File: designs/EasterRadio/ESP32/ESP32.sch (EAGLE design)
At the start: 25 parts, among them IC6 ESP32-WROVER-B, J3 S2B-NSHSS-TB, J5 S2B-NSHSS-TB

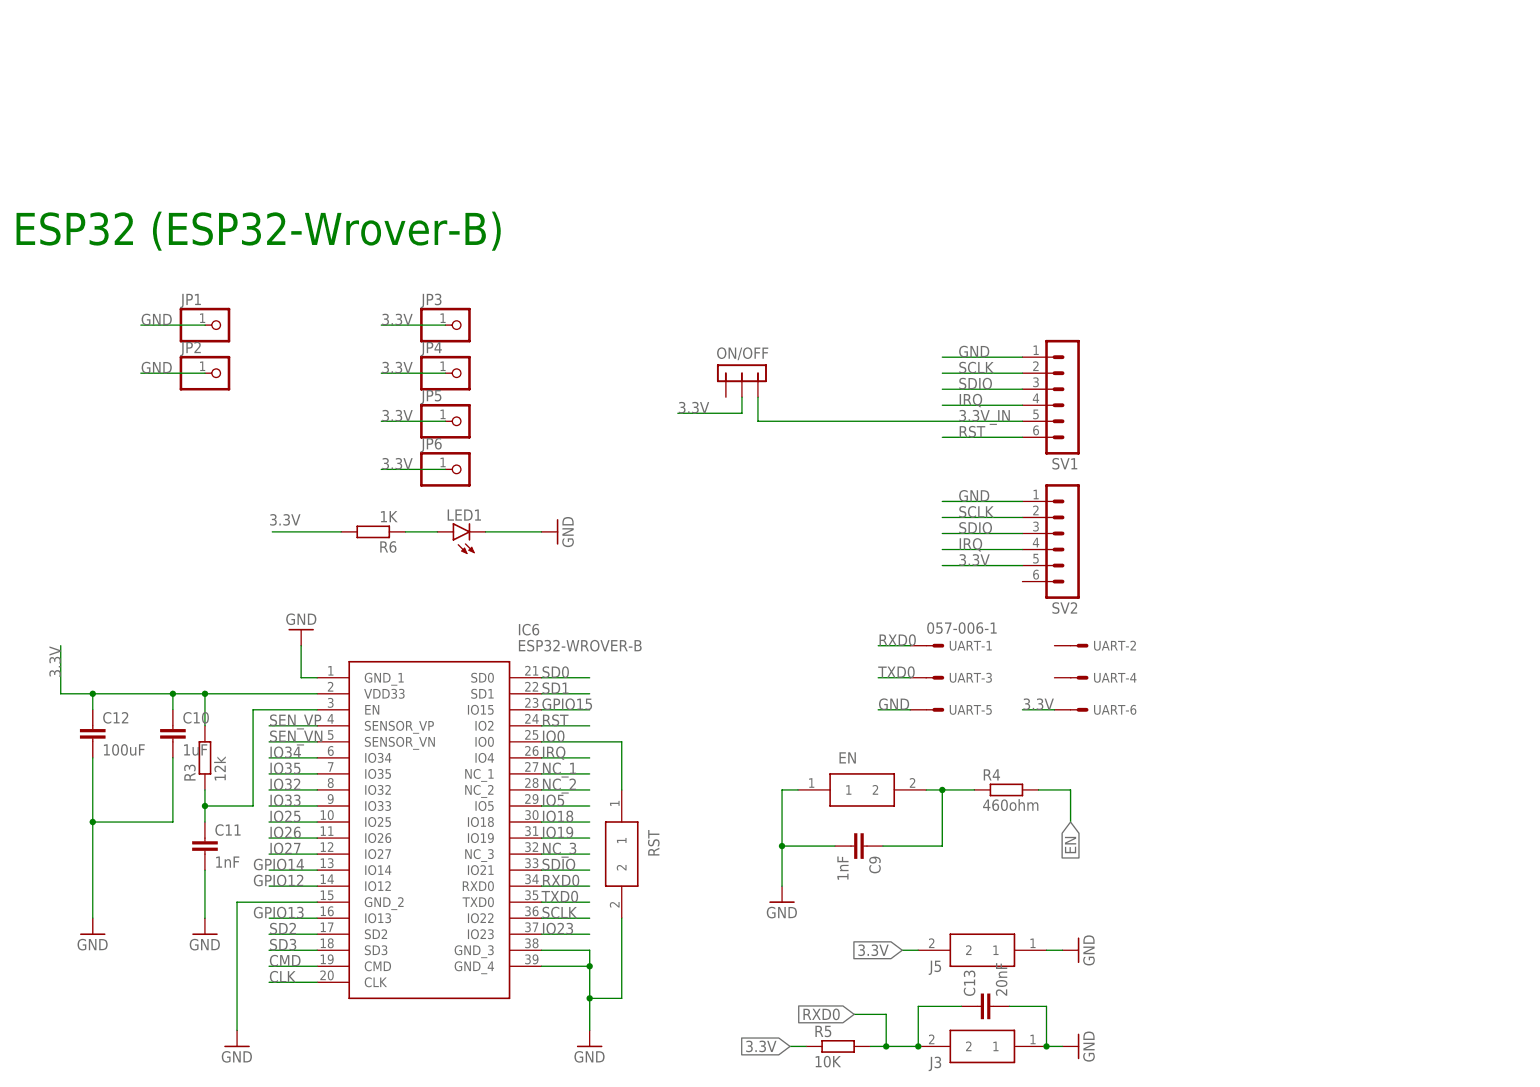
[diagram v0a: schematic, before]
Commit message: added ESP32 wrover E schematic
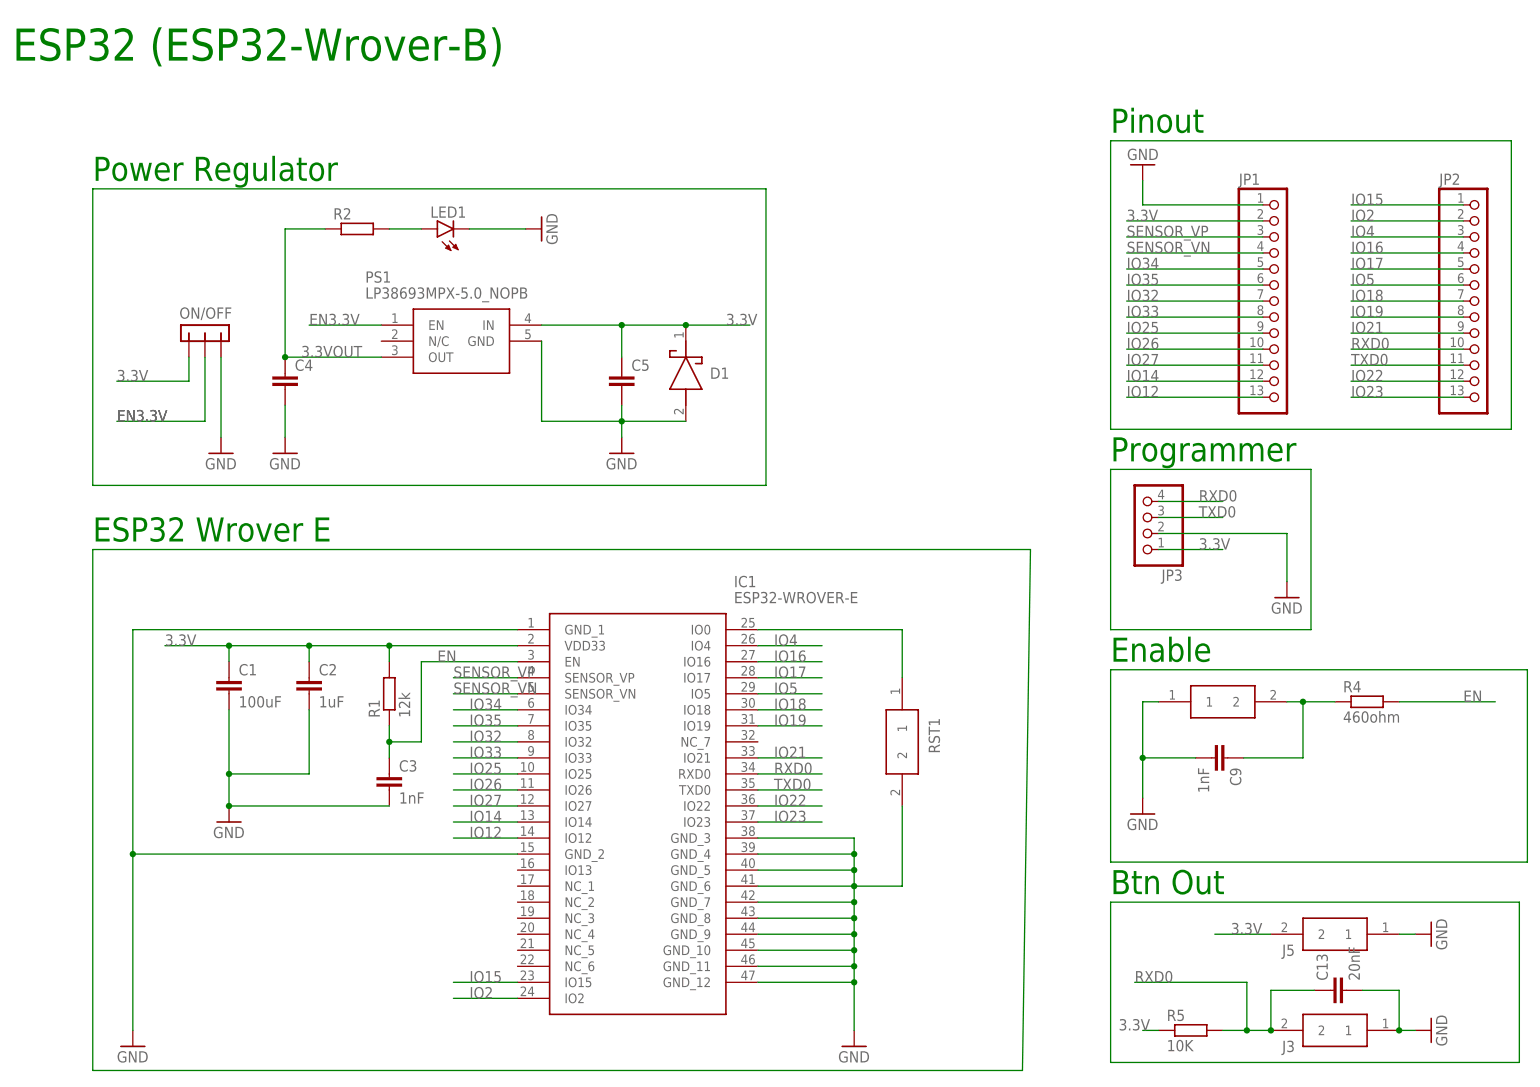
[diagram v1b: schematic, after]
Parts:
- removed C10: 1uF, CommonParts:C-EU_805C0805
- removed C11: 1nF, CommonParts:C-EU_805C0805
- removed C12: 100uF, CommonParts:C-EU_1206C1206
- removed IC6: ESP32-WROVER-B, ESP32-WROVER-B:ESP32-WROVER-B
- removed JP4, JP5, JP6: (no value), pinhead:PINHD-1X1
- removed R3: 12k, CommonParts:R-EU_805R0805
- removed R6: 1K, rcl:R-EU_R1206
- removed RST: FSMSMTR, FSMSMTR:FSMSMTR
- removed SV1, SV2: (no value), con-lstb:MA06-1
- removed UART: 057-006-1, con-panduit:057-006-1
- added C1: 100uF, CommonParts:C-EU_1206C1206
- added C2: 1uF, CommonParts:C-EU_805C0805
- added C3: 1nF, CommonParts:C-EU_805C0805
- added C4, C5: (no value), rcl:C-EUC0805
- added D1: LSM115JE3_TR13, CommonParts:LSM115JE3_TR13
- added IC1: ESP32-WROVER-E, MouserUseful:ESP32-WROVER-E
- added PS1: LP38693MPX-5.0_NOPB, MouserUseful:LP38693MPX-5.0_NOPB
- added R1: 12k, CommonParts:R-EU_805R0805
- added R2: (no value), rcl:R-EU_R0805
- added RST1: FSMSMTR, FSMSMTR:FSMSMTR
- JP1, JP2: device pinhead:PINHD-1X1 -> pinhead:PINHD-1X13
- JP3: device pinhead:PINHD-1X1 -> pinhead:PINHD-1X4/90
- LED1: device led:LEDSMT1206 -> CommonParts:LED_1206SMT1206
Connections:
- removed net 3.3V_IN: ON/OFF.1, SV1.5
- removed net CLK: IC6.CLK
- removed net CMD: IC6.CMD
- removed net GPIO12: IC6.IO12
- removed net GPIO13: IC6.IO13
- removed net GPIO14: IC6.IO14
- removed net GPIO15: IC6.IO15
- removed net IO0: IC6.IO0, RST.1
- removed net IRQ: IC6.IO4, SV1.4, SV2.4
- removed net N$14: LED1.A, R6.1
- removed net NC_1: IC6.NC_1
- removed net NC_2: IC6.NC_2
- removed net NC_3: IC6.NC_3
- removed net RST: IC6.IO2, SV1.6
- removed net SCLK: IC6.IO22, SV1.2, SV2.2
- removed net SD0: IC6.SD0
- removed net SD1: IC6.SD1
- removed net SD2: IC6.SD2
- removed net SD3: IC6.SD3
- removed net SDIO: IC6.IO21, SV1.3, SV2.3
- removed net SEN_VN: IC6.SENSOR_VN
- removed net SEN_VP: IC6.SENSOR_VP
- new net 3.3VOUT: C4.1, PS1.OUT, R2.1
- new net EN3.3V: ON/OFF.2, PS1.EN
- new net IO1: IC1.IO0, RST1.1
- new net IO12: IC1.IO12, JP1.13
- new net IO14: IC1.IO14, JP1.12
- new net IO15: IC1.IO15, JP2.1
- new net IO16: IC1.IO16, JP2.4
- new net IO17: IC1.IO17, JP2.5
- new net IO2: IC1.IO2, JP2.2
- new net IO21: IC1.IO21, JP2.9
- new net IO22: IC1.IO22, JP2.12
- new net IO4: IC1.IO4, JP2.3
- new net N$1: LED1.A, R2.2
- new net SENSOR_VN: IC1.SENSOR_VN, JP1.4
- new net SENSOR_VP: IC1.SENSOR_VP, JP1.3
- net 3.3V: now also C1.1, C2.1, C5.1, D1.K, IC1.VDD33, JP1.2, ON/OFF.3, PS1.IN, R1.2; no longer C10.1, C12.1, IC6.VDD33, JP4.1, JP5.1, JP6.1, ON/OFF.2, R3.2, R6.2, SV2.5, UART-6.S
- net EN: now also C3.1, IC1.EN, R1.1; no longer C11.1, IC6.EN, R3.1
- net GND: now also C1.2, C2.2, C3.2, C4.2, C5.2, D1.A, IC1.GND_1, IC1.GND_10, IC1.GND_11, IC1.GND_12, IC1.GND_2, IC1.GND_3, IC1.GND_4, IC1.GND_5, IC1.GND_6, IC1.GND_7, IC1.GND_8, IC1.GND_9, JP3.2, ON/OFF.1, PS1.GND, RST1.2; no longer C10.2, C11.2, C12.2, IC6.GND_1, IC6.GND_2, IC6.GND_3, IC6.GND_4, JP2.1, RST.2, SV1.1, SV2.1, UART-5.S
- net IO18: now also IC1.IO18, JP2.7; no longer IC6.IO18
- net IO19: now also IC1.IO19, JP2.8; no longer IC6.IO19
- net IO23: now also IC1.IO23, JP2.13; no longer IC6.IO23
- net IO25: now also IC1.IO25, JP1.9; no longer IC6.IO25
- net IO26: now also IC1.IO26, JP1.10; no longer IC6.IO26
- net IO27: now also IC1.IO27, JP1.11; no longer IC6.IO27
- net IO32: now also IC1.IO32, JP1.7; no longer IC6.IO32
- net IO33: now also IC1.IO33, JP1.8; no longer IC6.IO33
- net IO34: now also IC1.IO34, JP1.5; no longer IC6.IO34
- net IO35: now also IC1.IO35, JP1.6; no longer IC6.IO35
- net IO5: now also IC1.IO5, JP2.6; no longer IC6.IO5
- net RXD0: now also IC1.RXD0, JP2.10, JP3.4; no longer IC6.RXD0, UART-1.S
- net TXD0: now also IC1.TXD0, JP2.11, JP3.3; no longer IC6.TXD0, UART-3.S
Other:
- note added: "Btn Out"
- note added: "ESP32 Wrover E"
- note added: "Enable"
- note added: "Pinout"
- note added: "Power Regulator"
- note added: "Programmer"
- moved on the sheet: C13, C9, J3, J5, LED1, ON/OFF, R4, R5

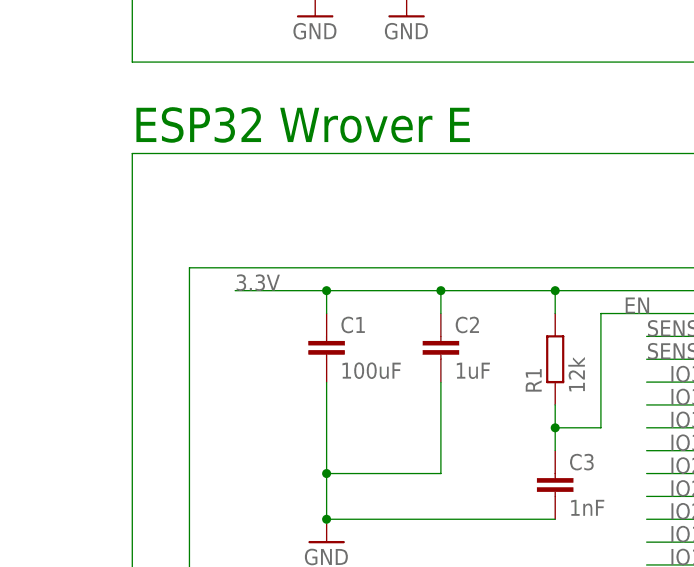
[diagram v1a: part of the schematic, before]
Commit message: added STM32 CAN to RS232 Adapter
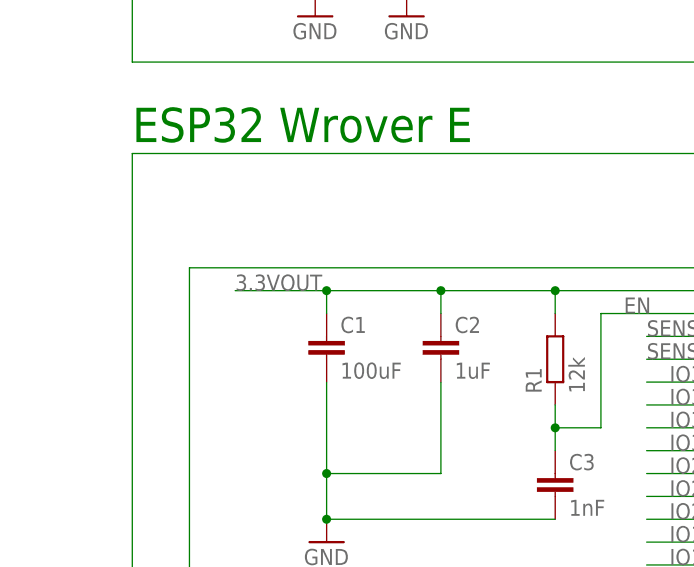
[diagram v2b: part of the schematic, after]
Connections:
- net 3.3V: no longer C1.1, C2.1, IC1.VDD33, R1.2
- net 3.3VOUT: now also C1.1, C2.1, IC1.VDD33, R1.2

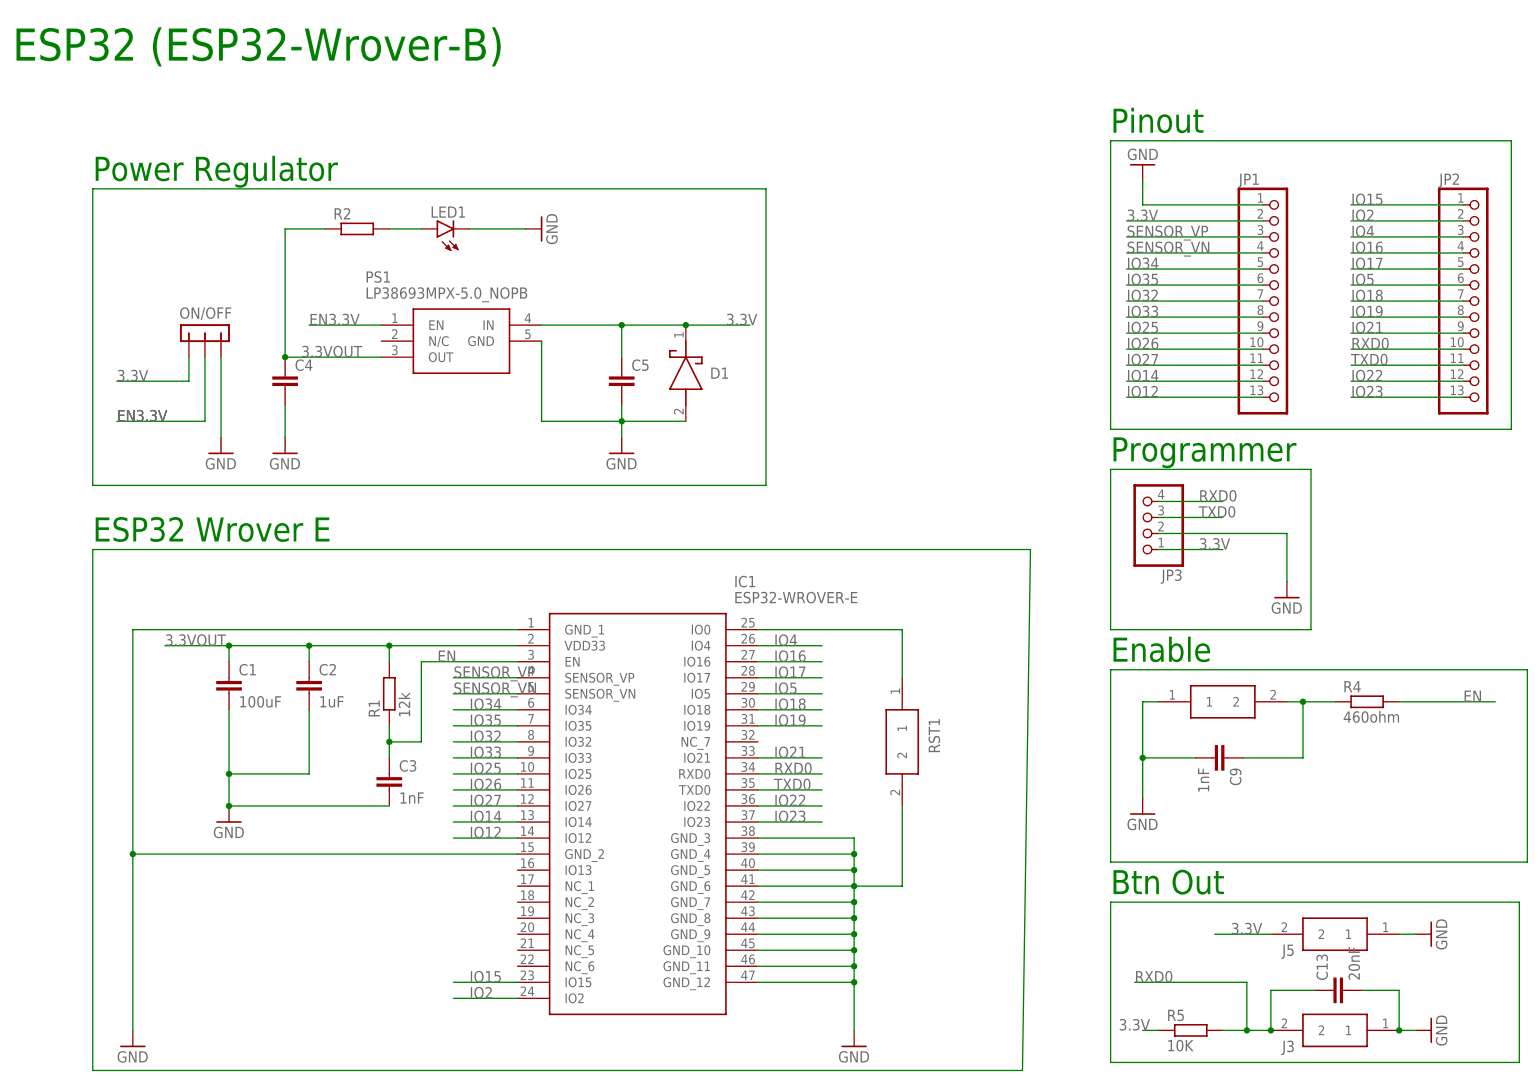
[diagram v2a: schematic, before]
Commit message: ESP32 brd layout
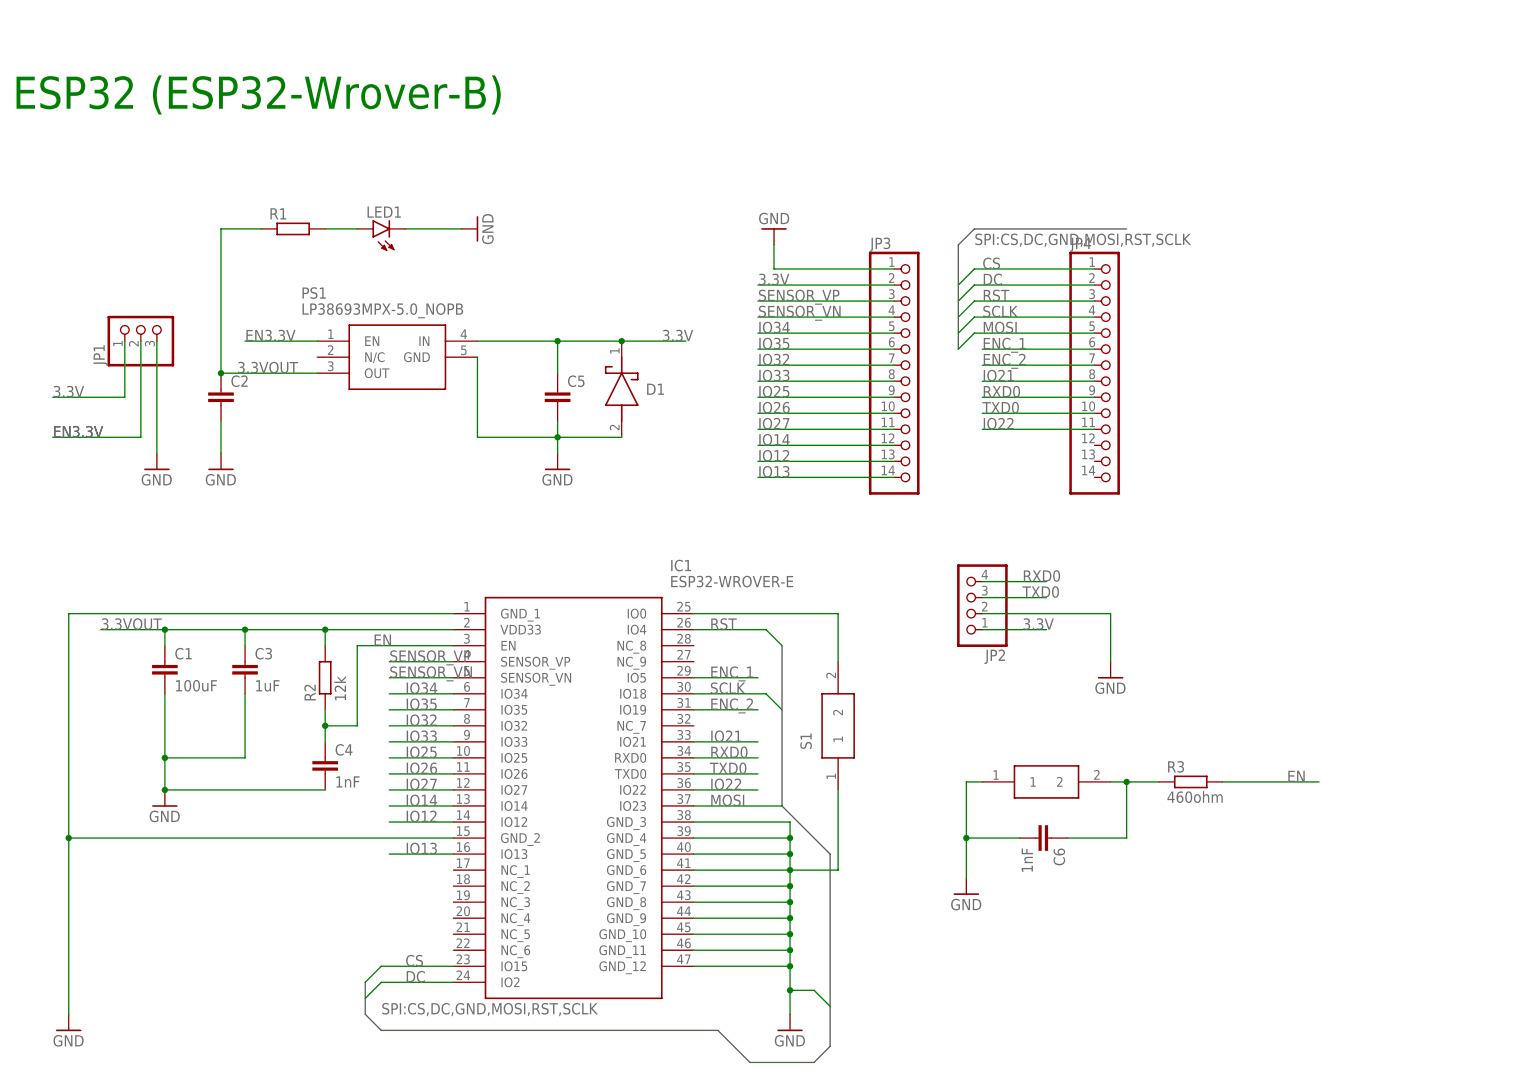
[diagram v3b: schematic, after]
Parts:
- removed C13: 20nF, CommonParts:C-EU_805C0805
- removed C9: 1nF, CommonParts:C-EU_805C0805
- removed EN, RST1: FSMSMTR, FSMSMTR:FSMSMTR
- removed J3, J5: S2B-NSHSS-TB, CommonParts:S2B-NSHSS-TB
- removed ON/OFF: -CON3, tango:-CON3
- removed R4: 460ohm, CommonParts:R-EU_805R0805
- removed R5: 10K, CommonParts:R-EU_1206R1206
- added C6: 1nF, CommonParts:C-EU_805C0805
- added JP4: (no value), pinhead:PINHD-1X14
- added R3: 460ohm, CommonParts:R-EU_805R0805
- added S1, S2: FSMSMTR, FSMSMTR:FSMSMTR
- C2: value 1uF -> (none); device CommonParts:C-EU_805C0805 -> rcl:C-EUC0805
- C3: value 1nF -> 1uF
- C4: value (none) -> 1nF; device rcl:C-EUC0805 -> CommonParts:C-EU_805C0805
- JP1: device pinhead:PINHD-1X13 -> pinhead:PINHD-1X3
- JP2: device pinhead:PINHD-1X13 -> pinhead:PINHD-1X4
- JP3: device pinhead:PINHD-1X4/90 -> pinhead:PINHD-1X14
- R1: value 12k -> (none); device CommonParts:R-EU_805R0805 -> rcl:R-EU_R0805
- R2: value (none) -> 12k; device rcl:R-EU_R0805 -> CommonParts:R-EU_805R0805
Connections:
- removed net IO15: IC1.IO15, JP2.1
- removed net IO16: IC1.IO16, JP2.4
- removed net IO17: IC1.IO17, JP2.5
- removed net IO18: IC1.IO18, JP2.7
- removed net IO19: IC1.IO19, JP2.8
- removed net IO2: IC1.IO2, JP2.2
- removed net IO23: IC1.IO23, JP2.13
- removed net IO4: IC1.IO4, JP2.3
- removed net IO5: IC1.IO5, JP2.6
- new net CS: IC1.IO15, JP4.1
- new net DC: IC1.IO2, JP4.2
- new net ENC_1: IC1.IO5, JP4.6
- new net ENC_2: IC1.IO19, JP4.7
- new net IO13: IC1.IO13, JP3.14
- new net MOSI: IC1.IO23, JP4.5
- new net RST: IC1.IO4, JP4.3
- new net SCLK: IC1.IO18, JP4.4
- net 3.3V: now also JP1.1, JP2.1, JP3.2; no longer J5.2, JP1.2, JP3.1, ON/OFF.3, R5.1
- net 3.3VOUT: now also C3.1, R1.1, R2.2; no longer C4.1, R1.2, R2.1
- net EN: now also C4.1, R2.1, R3.2; no longer C3.1, R1.1, R4.2
- net EN3.3V: now also JP1.2; no longer ON/OFF.2
- net EN_1: now also C6.1, R3.1, S2.2; no longer C9.1, EN.2, R4.1
- net GND: now also C6.2, JP1.3, JP2.2, JP3.1, S1.1, S2.1; no longer C13.2, C9.2, EN.1, J3.1, J5.1, JP1.1, JP3.2, ON/OFF.1, RST1.2
- net IO1: now also S1.2; no longer RST1.1
- net IO12: now also JP3.13; no longer JP1.13
- net IO14: now also JP3.12; no longer JP1.12
- net IO21: now also JP4.8; no longer JP2.9
- net IO22: now also JP4.11; no longer JP2.12
- net IO25: now also JP3.9; no longer JP1.9
- net IO26: now also JP3.10; no longer JP1.10
- net IO27: now also JP3.11; no longer JP1.11
- net IO32: now also JP3.7; no longer JP1.7
- net IO33: now also JP3.8; no longer JP1.8
- net IO34: now also JP3.5; no longer JP1.5
- net IO35: now also JP3.6; no longer JP1.6
- net N$1: now also R1.2; no longer R2.2
- net RXD0: now also JP2.4, JP4.9; no longer C13.1, J3.2, JP2.10, JP3.4, R5.2
- net SENSOR_VN: now also JP3.4; no longer JP1.4
- net SENSOR_VP: now also JP3.3; no longer JP1.3
- net TXD0: now also JP2.3, JP4.10; no longer JP2.11, JP3.3
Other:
- note removed: "Btn Out"
- note removed: "ESP32 Wrover E"
- note removed: "Enable"
- note removed: "Pinout"
- note removed: "Power Regulator"
- note removed: "Programmer"
- moved on the sheet: C1, C2, C3, C4, C5, D1, IC1, LED1, PS1, R1, R2
